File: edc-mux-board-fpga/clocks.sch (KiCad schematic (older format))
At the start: 22 parts, among them J1 OSC_PRG_HDR, U1 10CL040YF484I7G, U2 CDCE706, Y1 SiT1602BI-71-33E-48.000000

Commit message: changed shotkey diode to mosfet + controller
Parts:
- removed D1: 25V, Package_TO_SOT_SMD:SOT-323_SC-70, symbol Device:D_Small
- added C?: 10uF, symbol Device:C_Small
- added Q? (x2): CSD22206W, SW-Texas:DSBGA9, symbol SW-Texas:CSD22206W
- added R?: 470kΩ, symbol Device:R_Small_US
- added U?: LTC4412, Package_TO_SOT_SMD:TSOT-23-6, symbol SW-Linear:LTC4412
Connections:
- net labels added: +3.3V, +3V3USB, CLK0_FPGA, CLK1_CODEC, CLK2_CODEC, CLK3_MCU, CLK4_ETH
- net labels removed: CLK0, CLK1, CLK2, CLK3, CLK4
- wire segments 70 -> 94
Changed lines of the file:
@@
 Wire Wire Line
 	5100 2400 5100 2250
-$Comp
-L power:+3V3 #PWR05
-U 1 1 5CB4D740
-P 5100 1500
-F 0 "#PWR05" H 5100 1350 50  0001 C CNN
-F 1 "+3V3" H 5150 1700 50  0000 C CNN
-F 2 "" H 5100 1500 50  0001 C CNN
-F 3 "" H 5100 1500 50  0001 C CNN
-	1    5100 1500
-	1    0    0    -1
-$EndComp
 Text Notes 5300 4300 0    50   ~ 0
 Do I need a separate Reset connection\nto the MCU so it can reset the clock chips\nindependantly?
@@
 Wire Wire Line
 	2350 2250 2350 2600
-Text Notes 6600 3100 0    50   ~ 0
+Text Notes 6850 3100 0    50   ~ 0
 Y0 = 48MHz for FPGA\nY1 = 48MHz for CODECs\nY2 = 48MHz for CODECs\nY3 = for Microprocessor\nY4 = 25MHz for W5500 Ethernet
 $Comp
@@
 $EndComp
 Connection ~ 5100 2250
-Wire Wire Line
-	5100 1500 5100 1600
 Wire Wire Line
 	4300 2750 4400 2750
@@
 Wire Wire Line
 	3450 2550 3450 2650
-$Comp
-L Device:D_Small D1
-U 1 1 5CBBBA9E
-P 5100 1700
-F 0 "D1" V 5150 1600 50  0000 R CNN
-F 1 "25V" V 5100 1600 50  0000 R CNN
-F 2 "Package_TO_SOT_SMD:SOT-323_SC-70" V 5100 1700 50  0001 C CNN
-F 3 "~" V 5100 1700 50  0001 C CNN
-	1    5100 1700
-	0    -1   -1   0
-$EndComp
 Wire Wire Line
 	5100 2050 5100 2100
@@
 	3700 3500 4000 3500
 Text GLabel 6300 2750 2    50   Output ~ 0
-CLK0
+CLK0_FPGA
 Text GLabel 6300 2850 2    50   Output ~ 0
-CLK1
+CLK1_CODEC
 Text GLabel 6300 2950 2    50   Output ~ 0
-CLK2
+CLK2_CODEC
 Text GLabel 6300 3050 2    50   Output ~ 0
-CLK3
+CLK3_MCU
 Text GLabel 6300 3150 2    50   Output ~ 0
-CLK4
+CLK4_ETH
 Text GLabel 6300 3250 2    50   Output ~ 0
 CLK5
@@
 	5600 2100 5600 2150
 Connection ~ 5400 2100
-Wire Wire Line
-	5100 1800 5100 1850
 $Comp
 L power:GND #PWR07
@@
 AR Path="/5CC6CC1A/5CC6D47B/5CE98691" Ref="FB?"  Part="1"
 AR Path="/5CC3E5DC/5CE98691" Ref="FB1"  Part="1"
-F 0 "FB1" H 5200 2000 50  0000 L CNN
-F 1 "600Ω @ 100MHz" H 5200 1950 50  0000 L CNN
+F 0 "FB1" H 5000 2000 50  0000 R CNN
+F 1 "600Ω @ 100MHz" H 5000 1950 50  0000 R CNN
 F 2 "Capacitor_SMD:C_0805_2012Metric" V 5030 1950 50  0001 C CNN
 F 3 "~" H 5100 1950 50  0001 C CNN
@@
 	1    0    0    -1
 $EndComp
+$Comp
+L SW-Linear:LTC4412 U?
+U 1 1 5CC5E70E
+P 6550 1050
+AR Path="/5CAA362B/5CC5E70E" Ref="U?"  Part="1"
+AR Path="/5CC3E5DC/5CC5E70E" Ref="U?"  Part="1"
+F 0 "U?" H 6750 850 50  0000 C CNN
+F 1 "LTC4412" H 6500 1250 50  0000 C CNN
+F 2 "Package_TO_SOT_SMD:TSOT-23-6" H 6550 1350 50  0001 C CNN
+F 3 "https://www.analog.com/media/en/technical-documentation/data-sheets/4412fb.pdf" H 7100 1850 50  0001 C CNN
+F 4 "Linear Technologies" H 6550 1050 50  0001 C CNN "Manufacturer"
+F 5 "LTC4412HS6#TRMPBF" H 6550 1050 50  0001 C CNN "Manufacturers Part Number"
+	1    6550 1050
+	-1   0    0    -1
+$EndComp
+$Comp
+L power:+3.3V #PWR?
+U 1 1 5CC5E714
+P 5100 1050
+AR Path="/5CAA362B/5CC5E714" Ref="#PWR?"  Part="1"
+AR Path="/5CC3E5DC/5CC5E714" Ref="#PWR?"  Part="1"
+F 0 "#PWR?" H 5100 900 50  0001 C CNN
+F 1 "+3.3V" H 5100 1190 50  0000 C CNN
+F 2 "" H 5100 1050 50  0001 C CNN
+F 3 "" H 5100 1050 50  0001 C CNN
+	1    5100 1050
+	1    0    0    -1
+$EndComp
+$Comp
+L SW-Texas:CSD22206W Q?
+U 1 1 5CC5E71A
+P 5200 1350
+AR Path="/5CAA362B/5CC5E71A" Ref="Q?"  Part="1"
+AR Path="/5CC3E5DC/5CC5E71A" Ref="Q?"  Part="1"
+F 0 "Q?" H 5400 1400 50  0000 L CNN
+F 1 "CSD22206W" H 5400 1300 50  0000 L CNN
+F 2 "SW-Texas:DSBGA9" H 5400 1400 50  0001 C CNN
+F 3 "https://www.ti.com/lit/ds/symlink/csd22206w.pdf" H 5200 1350 50  0001 C CNN
+	1    5200 1350
+	-1   0    0    -1
+$EndComp
+Wire Wire Line
+	5100 1050 5100 1150
+Wire Wire Line
+	5100 1550 5100 1600
+Wire Wire Line
+	5400 1350 5550 1350
+Wire Wire Line
+	5550 1350 5550 950
+Wire Wire Line
+	5550 950  6100 950
+Text Label 6500 1600 0    50   ~ 0
++3V3USB
+$Comp
+L power:+3.3V #PWR?
+U 1 1 5CC5E726
+P 6950 750
+AR Path="/5CAA362B/5CC5E726" Ref="#PWR?"  Part="1"
+AR Path="/5CC3E5DC/5CC5E726" Ref="#PWR?"  Part="1"
+F 0 "#PWR?" H 6950 600 50  0001 C CNN
+F 1 "+3.3V" H 6950 890 50  0000 C CNN
+F 2 "" H 6950 750 50  0001 C CNN
+F 3 "" H 6950 750 50  0001 C CNN
+	1    6950 750
+	1    0    0    -1
+$EndComp
+Wire Wire Line
+	6950 750  6950 950
+Wire Wire Line
+	5100 1600 5600 1600
+Wire Wire Line
+	5700 1600 5700 1250
+Wire Wire Line
+	5700 1050 6100 1050
+Connection ~ 5100 1600
+$Comp
+L SW-Texas:CSD22206W Q?
+U 1 1 5CC5E732
+P 6000 1500
+AR Path="/5CAA362B/5CC5E732" Ref="Q?"  Part="1"
+AR Path="/5CC3E5DC/5CC5E732" Ref="Q?"  Part="1"
+F 0 "Q?" V 6300 1500 50  0000 C CNN
+F 1 "CSD22206W" V 6400 1500 50  0000 C CNN
+F 2 "SW-Texas:DSBGA9" H 6200 1550 50  0001 C CNN
+F 3 "https://www.ti.com/lit/ds/symlink/csd22206w.pdf" H 6000 1500 50  0001 C CNN
+	1    6000 1500
+	0    1    1    0
+$EndComp
+Wire Wire Line
+	5700 1600 5800 1600
+Connection ~ 5700 1600
+Wire Wire Line
+	6200 1600 6500 1600
+Wire Wire Line
+	6100 1150 6000 1150
+Wire Wire Line
+	6000 1150 6000 1250
+$Comp
+L Device:R_Small_US R?
+U 1 1 5CC5E73D
+P 5850 1250
+AR Path="/5CAA362B/5CC5E73D" Ref="R?"  Part="1"
+AR Path="/5CC3E5DC/5CC5E73D" Ref="R?"  Part="1"
+F 0 "R?" H 5880 1270 50  0000 L CNN
+F 1 "470kΩ" H 5880 1210 50  0000 L CNN
+F 2 "" H 5850 1250 50  0001 C CNN
+F 3 "~" H 5850 1250 50  0001 C CNN
+	1    5850 1250
+	0    1    1    0
+$EndComp
+Wire Wire Line
+	5750 1250 5700 1250
+Connection ~ 5700 1250
+Wire Wire Line
+	5700 1250 5700 1050
+Wire Wire Line
+	5950 1250 6000 1250
+Connection ~ 6000 1250
+Wire Wire Line
+	6000 1250 6000 1300
+$Comp
+L power:GND #PWR?
+U 1 1 5CC5E749
+P 7150 2000
+AR Path="/5CAA362B/5CC5E749" Ref="#PWR?"  Part="1"
+AR Path="/5CC3E5DC/5CC5E749" Ref="#PWR?"  Part="1"
+F 0 "#PWR?" H 7150 1750 50  0001 C CNN
+F 1 "GND" H 7150 1850 50  0000 C CNN
+F 2 "" H 7150 2000 50  0001 C CNN
+F 3 "" H 7150 2000 50  0001 C CNN
+	1    7150 2000
+	1    0    0    -1
+$EndComp
+Wire Wire Line
+	6950 1050 7150 1050
+Wire Wire Line
+	7150 1050 7150 1150
+Wire Wire Line
+	6950 1150 7150 1150
+Connection ~ 7150 1150
+Wire Wire Line
+	7150 1150 7150 1850
+$Comp
+L Device:C_Small C?
+U 1 1 5CC5E754
+P 5600 1700
+AR Path="/5CAA362B/5CC5E754" Ref="C?"  Part="1"
+AR Path="/5CC3E5DC/5CC5E754" Ref="C?"  Part="1"
+F 0 "C?" H 5700 1750 50  0000 L CNN
+F 1 "10uF" H 5700 1700 50  0000 L CNN
+F 2 "" H 5600 1700 50  0001 C CNN
+F 3 "~" H 5600 1700 50  0001 C CNN
+	1    5600 1700
+	-1   0    0    -1
+$EndComp
+Connection ~ 5600 1600
+Wire Wire Line
+	5600 1600 5700 1600
+Wire Wire Line
+	5100 1600 5100 1850
+Wire Wire Line
+	5600 1800 5600 1850
+Wire Wire Line
+	5600 1850 7150 1850
+Connection ~ 7150 1850
+Wire Wire Line
+	7150 1850 7150 2000
 $EndSCHEMATC

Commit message: More work on CODEC - FPGA connections
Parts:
- removed U1: 10CL040YF484I7G, SW-Intel:FBGA-484_23.0x23.0mm_Layout22x22_P1.0mm, symbol SW-Intel:10CL040YF484I7G
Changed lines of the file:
@@
 $Descr A4 11693 8268
 encoding utf-8
-Sheet 3 23
+Sheet 3 25
 Title ""
 Date ""
@@
 All Clocks are LVCMOS 3.3V
 $Comp
-L SW-Intel:10CL040YF484I7G U1
-U 4 1 5CB15687
-P 9400 2650
-F 0 "U1" H 9850 2750 50  0000 L CNN
-F 1 "10CL040YF484I7G" H 9850 2650 50  0000 L CNN
-F 2 "SW-Intel:FBGA-484_23.0x23.0mm_Layout22x22_P1.0mm" H 12100 3550 50  0001 C CNN
-F 3 "https://www.intel.com/content/www/us/en/programmable/products/fpga/cyclone-series/cyclone-10/cyclone-10-lp/support.html" H 12100 3550 50  0001 C CNN
-	4    9400 2650
-	1    0    0    -1
-$EndComp
-$Comp
 L Device:R_Small_US R2

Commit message: unannotated components after major changes
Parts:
- renumbered C1 to C?, C3 to C?, C2 to C?, FB1 to FB?, J1 to J?, R2 to R?, R1 to R?, R3 to R?, R6 to R?, R10 to R?, R11 to R?, R13 to R?, R4 to R?, R5 to R?, R7 to R?, R8 to R?, R9 to R?, R12 to R?, U2 to U?, Y1 to Y?
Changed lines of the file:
@@
 All Clocks are LVCMOS 3.3V
 $Comp
-L Device:R_Small_US R2
+L Device:R_Small_US R?
 U 1 1 5CB400FD
 P 4300 2500
-F 0 "R2" H 4400 2550 50  0000 L CNN
+F 0 "R?" H 4400 2550 50  0000 L CNN
 F 1 "10kΩ" H 4400 2500 50  0000 L CNN
 F 2 "Resistor_SMD:R_0402_1005Metric" H 4300 2500 50  0001 C CNN
@@
 Connection ~ 4300 2750
 $Comp
-L Device:R_Small_US R1
+L Device:R_Small_US R?
 U 1 1 5CB46AF9
 P 4200 2500
-F 0 "R1" H 4100 2550 50  0000 R CNN
+F 0 "R?" H 4100 2550 50  0000 R CNN
 F 1 "10kΩ" H 4100 2500 50  0000 R CNN
 F 2 "Resistor_SMD:R_0402_1005Metric" H 4200 2500 50  0001 C CNN
@@
 Do I need a separate Reset connection\nto the MCU so it can reset the clock chips\nindependantly?
 $Comp
-L power:GND #PWR012
+L power:GND #PWR?
 U 1 1 5CB6F7AE
 P 5100 3800
-F 0 "#PWR012" H 5100 3550 50  0001 C CNN
+F 0 "#PWR?" H 5100 3550 50  0001 C CNN
 F 1 "GND" H 5150 3600 50  0000 C CNN
 F 2 "" H 5100 3800 50  0001 C CNN
@@
 	5100 3800 5100 3500
 $Comp
-L Device:R_Small_US R3
+L Device:R_Small_US R?
 U 1 1 5CB77FB9
 P 1950 2550
-F 0 "R3" H 1850 2600 50  0000 R CNN
+F 0 "R?" H 1850 2600 50  0000 R CNN
 F 1 "1kΩ" H 1850 2550 50  0000 R CNN
 F 2 "Resistor_SMD:R_0402_1005Metric" H 1950 2550 50  0001 C CNN
@@
 $EndComp
 $Comp
-L Device:C_Small C1
+L Device:C_Small C?
 U 1 1 5CB7C30C
 P 2600 2250
-F 0 "C1" V 2350 2250 50  0000 C CNN
+F 0 "C?" V 2350 2250 50  0000 C CNN
 F 1 "100nF" V 2450 2250 50  0000 C CNN
 F 2 "Capacitor_SMD:C_0603_1608Metric" H 2600 2250 50  0001 C CNN
@@
 	2350 2250 2500 2250
 $Comp
-L power:GND #PWR06
+L power:GND #PWR?
 U 1 1 5CB7F01E
 P 2700 2400
-F 0 "#PWR06" H 2700 2150 50  0001 C CNN
+F 0 "#PWR?" H 2700 2150 50  0001 C CNN
 F 1 "GND" H 2750 2200 50  0000 C CNN
 F 2 "" H 2700 2400 50  0001 C CNN
@@
 $EndComp
 $Comp
-L power:GND #PWR010
+L power:GND #PWR?
 U 1 1 5CB809B1
 P 2350 3450
-F 0 "#PWR010" H 2350 3200 50  0001 C CNN
+F 0 "#PWR?" H 2350 3200 50  0001 C CNN
 F 1 "GND" H 2400 3250 50  0000 C CNN
 F 2 "" H 2350 3450 50  0001 C CNN
@@
 	1950 2950 1950 2650
 $Comp
-L SW-SiTime:SiT1602B Y1
+L SW-SiTime:SiT1602B Y?
 U 1 1 5CAC6025
 P 2350 2950
-F 0 "Y1" H 2550 2650 50  0000 R CNN
+F 0 "Y?" H 2550 2650 50  0000 R CNN
 F 1 "SiT1602BI-71-33E-48.000000" H 2000 2750 50  0000 R CNN
 F 2 "Crystal:Crystal_SMD_2016-4Pin_2.0x1.6mm" H 2200 4850 50  0001 C CNN
@@
 Y0 = 48MHz for FPGA\nY1 = 48MHz for CODECs\nY2 = 48MHz for CODECs\nY3 = for Microprocessor\nY4 = 25MHz for W5500 Ethernet
 $Comp
-L SW-Texas:CDCE706 U2
+L SW-Texas:CDCE706 U?
 U 1 1 5CB9BD83
 P 5100 3000
-F 0 "U2" H 5450 2650 50  0000 C CNN
+F 0 "U?" H 5450 2650 50  0000 C CNN
 F 1 "CDCE706" H 4700 3350 50  0000 C CNN
 F 2 "Package_SO:TSSOP-20_4.4x6.5mm_P0.65mm" H 4300 3900 50  0001 C CNN
@@
 	2700 2950 2850 2950
 $Comp
-L Device:R_Small_US R6
+L Device:R_Small_US R?
 U 1 1 5CBA8CC0
 P 2950 2950
-F 0 "R6" V 3100 2950 50  0000 C CNN
+F 0 "R?" V 3100 2950 50  0000 C CNN
 F 1 "0Ω" V 3200 2950 50  0000 C CNN
 F 2 "Resistor_SMD:R_0402_1005Metric" H 2950 2950 50  0001 C CNN
@@
 $EndComp
 $Comp
-L Device:R_Small_US R10
+L Device:R_Small_US R?
 U 1 1 5CBAC0C1
 P 3200 3250
-F 0 "R10" H 3300 3300 50  0000 L CNN
+F 0 "R?" H 3300 3300 50  0000 L CNN
 F 1 "1kΩ" H 3300 3250 50  0000 L CNN
 F 2 "Resistor_SMD:R_0402_1005Metric" H 3200 3250 50  0001 C CNN
@@
 	3200 3050 3200 3150
 $Comp
-L power:GND #PWR011
+L power:GND #PWR?
 U 1 1 5CBADCB5
 P 3200 3550
-F 0 "#PWR011" H 3200 3300 50  0001 C CNN
+F 0 "#PWR?" H 3200 3300 50  0001 C CNN
 F 1 "GND" H 3250 3350 50  0000 C CNN
 F 2 "" H 3200 3550 50  0001 C CNN
@@
 	3050 2950 4400 2950
 $Comp
-L Connector_Generic:Conn_01x04 J1
+L Connector_Generic:Conn_01x04 J?
 U 1 1 5CBAFEA0
 P 3250 2350
-F 0 "J1" H 3150 2700 50  0000 C CNN
+F 0 "J?" H 3150 2700 50  0000 C CNN
 F 1 "OSC_PRG_HDR" H 3150 2600 50  0000 C CNN
 F 2 "Connector_PinHeader_2.54mm:PinHeader_1x04_P2.54mm_Vertical" H 3250 2350 50  0001 C CNN
@@
 	3450 2250 4050 2250
 $Comp
-L power:GND #PWR08
+L power:GND #PWR?
 U 1 1 5CBB95F3
 P 3450 2650
-F 0 "#PWR08" H 3450 2400 50  0001 C CNN
+F 0 "#PWR?" H 3450 2400 50  0001 C CNN
 F 1 "GND" H 3500 2450 50  0000 C CNN
 F 2 "" H 3450 2650 50  0001 C CNN
@@
 Default:\nS0 pulled down: entire chip powered down\nS1 pulled down: outputs are switched to low state\nThus pull high to enable device\n
 $Comp
-L Device:R_Small_US R11
+L Device:R_Small_US R?
 U 1 1 5CBC030E
 P 3700 3250
-F 0 "R11" H 3800 3300 50  0000 L CNN
+F 0 "R?" H 3800 3300 50  0000 L CNN
 F 1 "1kΩ" H 3800 3250 50  0000 L CNN
 F 2 "Resistor_SMD:R_0402_1005Metric" H 3700 3250 50  0001 C CNN
@@
 $EndComp
 $Comp
-L Device:R_Small_US R13
+L Device:R_Small_US R?
 U 1 1 5CBC0B41
 P 4000 3350
-F 0 "R13" H 4100 3400 50  0000 L CNN
+F 0 "R?" H 4100 3400 50  0000 L CNN
 F 1 "1kΩ" H 4100 3350 50  0000 L CNN
 F 2 "Resistor_SMD:R_0402_1005Metric" H 4000 3350 50  0001 C CNN
@@
 	4000 3250 4400 3250
 $Comp
-L power:+3V3 #PWR09
+L power:+3V3 #PWR?
 U 1 1 5CBC31FA
 P 3550 3300
-F 0 "#PWR09" H 3550 3150 50  0001 C CNN
+F 0 "#PWR?" H 3550 3150 50  0001 C CNN
 F 1 "+3V3" H 3600 3500 50  0000 C CNN
 F 2 "" H 3550 3300 50  0001 C CNN
@@
 CLK5
 $Comp
-L Device:R_Small_US R4
+L Device:R_Small_US R?
 U 1 1 5CBCD139
 P 6000 2750
-F 0 "R4" V 5950 2600 50  0000 C CNN
+F 0 "R?" V 5950 2600 50  0000 C CNN
 F 1 "5Ω" V 5950 2900 50  0000 C CNN
 F 2 "Resistor_SMD:R_0402_1005Metric" H 6000 2750 50  0001 C CNN
@@
 $EndComp
 $Comp
-L Device:R_Small_US R5
+L Device:R_Small_US R?
 U 1 1 5CBCE005
 P 6000 2850
-F 0 "R5" V 5950 2700 50  0000 C CNN
+F 0 "R?" V 5950 2700 50  0000 C CNN
 F 1 "5Ω" V 5950 3000 50  0000 C CNN
 F 2 "Resistor_SMD:R_0402_1005Metric" H 6000 2850 50  0001 C CNN
@@
 $EndComp
 $Comp
-L Device:R_Small_US R7
+L Device:R_Small_US R?
 U 1 1 5CBCE2A6
 P 6000 2950
-F 0 "R7" V 5950 2800 50  0000 C CNN
+F 0 "R?" V 5950 2800 50  0000 C CNN
 F 1 "5Ω" V 5950 3100 50  0000 C CNN
 F 2 "Resistor_SMD:R_0402_1005Metric" H 6000 2950 50  0001 C CNN
@@
 $EndComp
 $Comp
-L Device:R_Small_US R8
+L Device:R_Small_US R?
 U 1 1 5CBCE616
 P 6000 3050
-F 0 "R8" V 5950 2900 50  0000 C CNN
+F 0 "R?" V 5950 2900 50  0000 C CNN
 F 1 "5Ω" V 5950 3200 50  0000 C CNN
 F 2 "Resistor_SMD:R_0402_1005Metric" H 6000 3050 50  0001 C CNN
@@
 $EndComp
 $Comp
-L Device:R_Small_US R9
+L Device:R_Small_US R?
 U 1 1 5CBCE913
 P 6000 3150
-F 0 "R9" V 5950 3000 50  0000 C CNN
+F 0 "R?" V 5950 3000 50  0000 C CNN
 F 1 "5Ω" V 5950 3300 50  0000 C CNN
 F 2 "Resistor_SMD:R_0402_1005Metric" H 6000 3150 50  0001 C CNN
@@
 $EndComp
 $Comp
-L Device:R_Small_US R12
+L Device:R_Small_US R?
 U 1 1 5CBCEA5B
 P 6000 3250
-F 0 "R12" V 5950 3100 50  0000 C CNN
+F 0 "R?" V 5950 3100 50  0000 C CNN
 F 1 "5Ω" V 5950 3400 50  0000 C CNN
 F 2 "Resistor_SMD:R_0402_1005Metric" H 6000 3250 50  0001 C CNN
@@
 	6100 2750 6300 2750
 $Comp
-L Device:C_Small C3
+L Device:C_Small C?
 U 1 1 5CBDE920
 P 5600 2250
-F 0 "C3" H 5500 2200 50  0000 R CNN
+F 0 "C?" H 5500 2200 50  0000 R CNN
 F 1 "100nF" H 5500 2250 50  0000 R CNN
 F 2 "Capacitor_SMD:C_0603_1608Metric" H 5600 2250 50  0001 C CNN
@@
 $EndComp
 $Comp
-L Device:C_Small C2
+L Device:C_Small C?
 U 1 1 5CBE047E
 P 5400 2250
-F 0 "C2" H 5550 2200 50  0000 R CNN
+F 0 "C?" H 5550 2200 50  0000 R CNN
 F 1 "100nF" H 5650 2300 50  0000 R CNN
 F 2 "Capacitor_SMD:C_0603_1608Metric" H 5400 2250 50  0001 C CNN
@@
 Connection ~ 5400 2100
 $Comp
-L power:GND #PWR07
+L power:GND #PWR?
 U 1 1 5CBE6F18
 P 5500 2400
-F 0 "#PWR07" H 5500 2150 50  0001 C CNN
+F 0 "#PWR?" H 5500 2150 50  0001 C CNN
 F 1 "GND" H 5550 2200 50  0000 C CNN
 F 2 "" H 5500 2400 50  0001 C CNN
@@
 P 5100 1950
 AR Path="/5CC6CC1A/5CC6D47B/5CE98691" Ref="FB?"  Part="1"
-AR Path="/5CC3E5DC/5CE98691" Ref="FB1"  Part="1"
-F 0 "FB1" H 5000 2000 50  0000 R CNN
+AR Path="/5CC3E5DC/5CE98691" Ref="FB?"  Part="1"
+F 0 "FB?" H 5000 2000 50  0000 R CNN
 F 1 "600Ω @ 100MHz" H 5000 1950 50  0000 R CNN
 F 2 "Capacitor_SMD:C_0805_2012Metric" V 5030 1950 50  0001 C CNN

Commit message: Finished FPGA and MCU interconnections.
Finished up interrupt wiring
Fixed a few missing connections
Annotated Schematic
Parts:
- gave numbers to parts that had none: 25
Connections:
- no-connect marks 0 -> 1

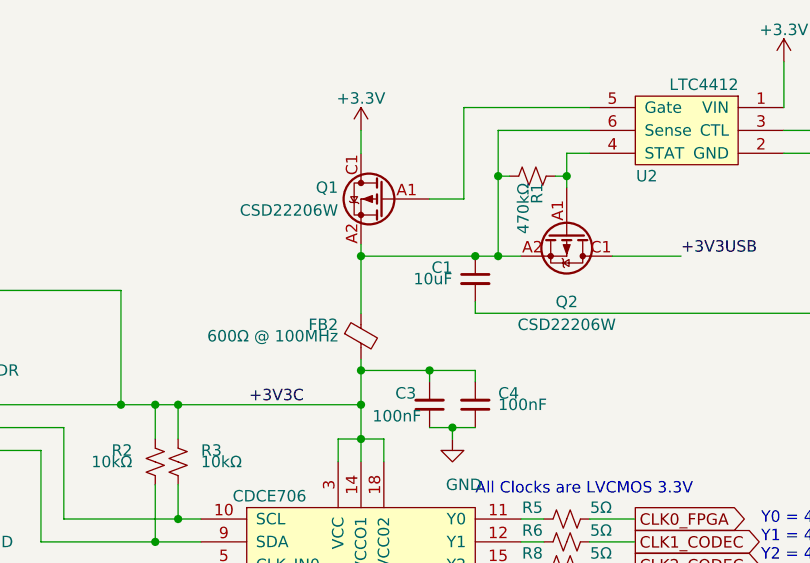
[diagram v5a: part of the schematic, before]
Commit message: assigned more footprints
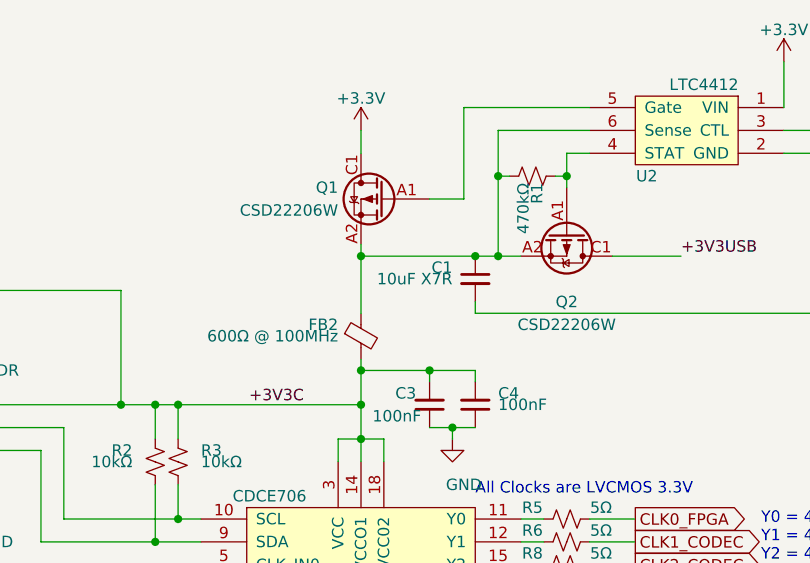
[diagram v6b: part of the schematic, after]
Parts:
- C1: value 10uF -> 10uF X7R; footprint (none) -> Capacitor_SMD:C_1206_3216Metric; Manufacturer (none) -> Kemet; Manufacturers Part Number (none) -> C1206C106J3RACAUTO; Package ID (none) -> 1206in/3216mm
- R1: footprint (none) -> Resistor_SMD:R_0402_1005Metric
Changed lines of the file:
@@
 F 0 "R1" H 5880 1270 50  0000 L CNN
 F 1 "470kΩ" H 5880 1210 50  0000 L CNN
-F 2 "" H 5850 1250 50  0001 C CNN
+F 2 "Resistor_SMD:R_0402_1005Metric" H 5850 1250 50  0001 C CNN
 F 3 "~" H 5850 1250 50  0001 C CNN
 	1    5850 1250
@@
 AR Path="/5CC3E5DC/5CC5E754" Ref="C1"  Part="1"
 F 0 "C1" H 5700 1750 50  0000 L CNN
-F 1 "10uF" H 5700 1700 50  0000 L CNN
-F 2 "" H 5600 1700 50  0001 C CNN
+F 1 "10uF X7R" H 5700 1700 50  0000 L CNN
+F 2 "Capacitor_SMD:C_1206_3216Metric" H 5600 1700 50  0001 C CNN
 F 3 "~" H 5600 1700 50  0001 C CNN
+F 4 "Kemet" H 0   0   50  0001 C CNN "Manufacturer"
+F 5 "C1206C106J3RACAUTO" H 0   0   50  0001 C CNN "Manufacturers Part Number"
+F 6 "1206in/3216mm" H 0   0   50  0001 C CNN "Package ID"
 	1    5600 1700
 	-1   0    0    -1

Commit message: re-annotating after adding power ICs and decoupling capacitors.
Also verified most footprints, and updated schematic field data.
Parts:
- C112: renamed from C2; value 100nF -> 100nF X7R
- C113: renamed from C3; value 100nF -> 100nF X7R
- C115: renamed from C4; value 100nF -> 100nF X7R
- R1: renamed from R4; Package ID (none) -> 0402in/1005mm
- R10: renamed from R6; Package ID (none) -> 0402in/1005mm
- R11: renamed from R8; Package ID (none) -> 0402in/1005mm
- R12: renamed from R9; Package ID (none) -> 0402in/1005mm
- R13: renamed from R10; Package ID (none) -> 0402in/1005mm
- R14: renamed from R13; Package ID (none) -> 0402in/1005mm
- R2: renamed from R7; Package ID (none) -> 0402in/1005mm
- R3: renamed from R11; Package ID (none) -> 0402in/1005mm
- R4: renamed from R12; Package ID (none) -> 0402in/1005mm
- R5: renamed from R14; Package ID (none) -> 0402in/1005mm
- R6: renamed from R2; Package ID (none) -> 0402in/1005mm
- R7: renamed from R3; Package ID (none) -> 0402in/1005mm
- R8: renamed from R1; Package ID (none) -> 0402in/1005mm
- R9: renamed from R5; Package ID (none) -> 0402in/1005mm
- U7: renamed from U3; Description (none) -> Programmable Clock Generator; Manufacturer (none) -> Texas Instruments; Manufacturers Part Number (none) -> CDCE706; Package ID (none) -> TSSOP20
- renumbered C1 to C114, FB2 to FB3, U2 to U8
